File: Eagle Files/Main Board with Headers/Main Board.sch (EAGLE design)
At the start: 34 parts, among them Y1 16MHz

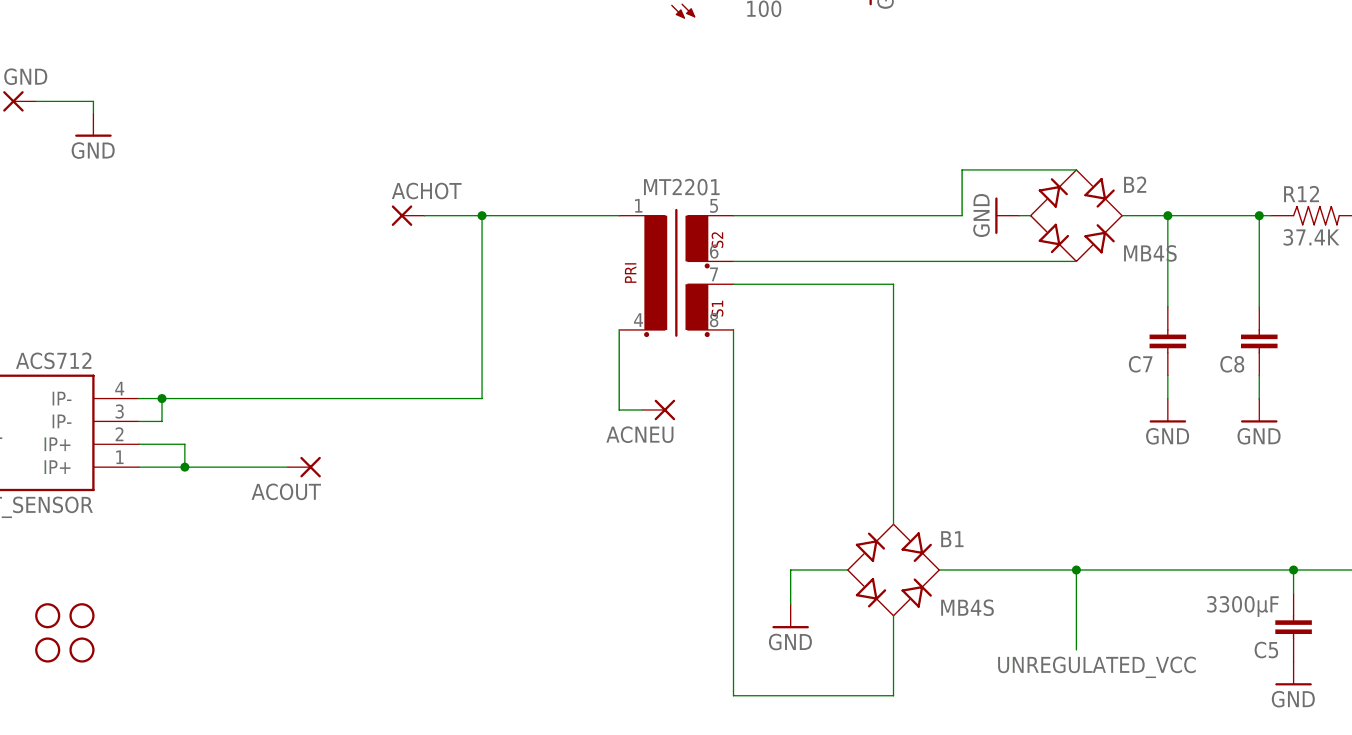
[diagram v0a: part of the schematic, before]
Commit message: More updates to the Main Board with Headers.
The transformer will now be under the board, so now we can place things inside that footprint on the top.

This saves us something around a square inch or two of board space.

--Arthur

git-svn-id: http://cd-net.net/CPE496/trunk@95 05b6d0e0-c345-4a8e-a5b7-579c8bd0b646
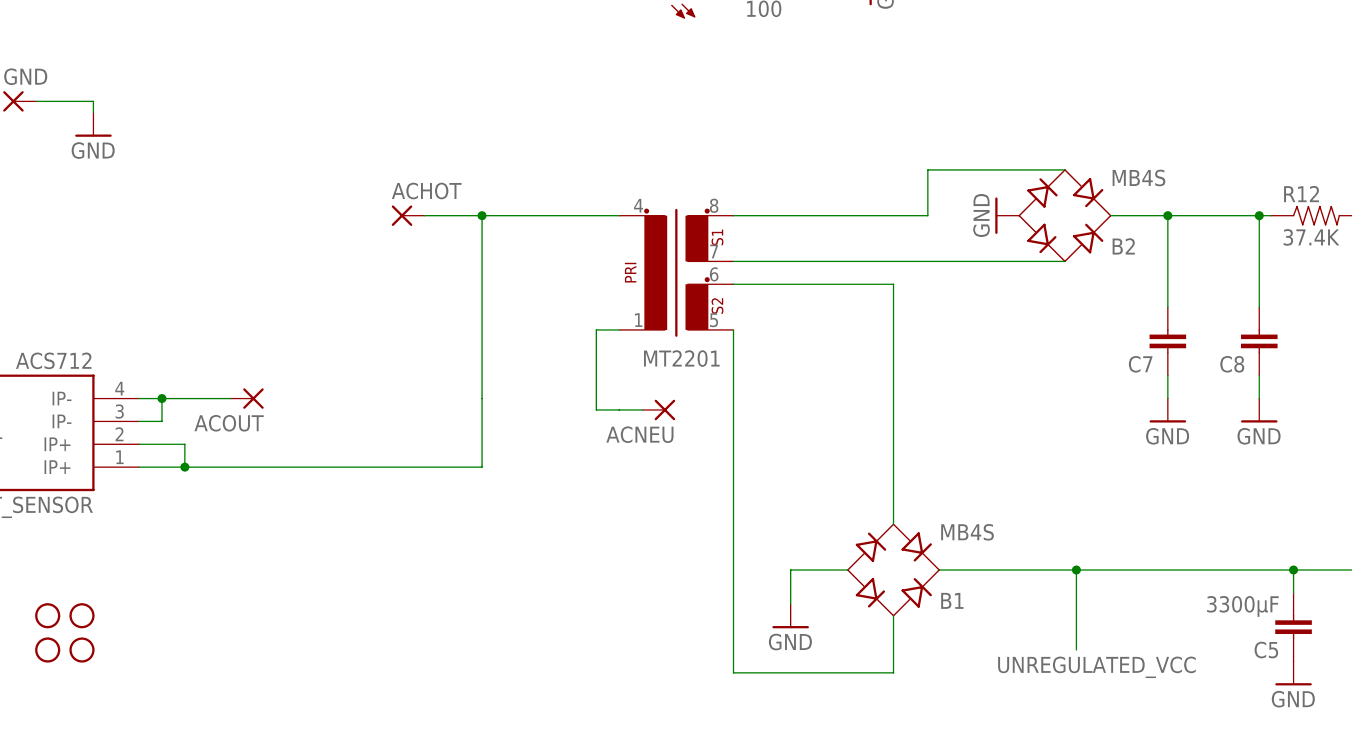
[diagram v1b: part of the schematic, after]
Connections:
- removed net N$8: ACOUT.P, CURRENT_SENSOR.IP+@1, CURRENT_SENSOR.IP+@2
- new net N$9: ACOUT.P, CURRENT_SENSOR.IP-@3, CURRENT_SENSOR.IP-@4
- net N$1: now also CURRENT_SENSOR.IP+@1, CURRENT_SENSOR.IP+@2, MT2201.4; no longer CURRENT_SENSOR.IP-@3, CURRENT_SENSOR.IP-@4, MT2201.1
- net N$2: now also MT2201.1; no longer MT2201.4
- net N$23: now also B1.AC2, MT2201.6; no longer B1.AC1, MT2201.7
- net N$3: now also B1.AC1, MT2201.5; no longer B1.AC2, MT2201.8
- net N$4: now also MT2201.7; no longer MT2201.5
- net N$5: now also MT2201.8; no longer MT2201.6
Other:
- moved on the sheet: ACOUT, B1, B2, MT2201
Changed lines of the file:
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@@
 <setting verticaltext="up"/>
 </settings>
-<grid distance="0.1" unitdist="inch" unit="inch" style="lines" multiple="1" display="no" altdistance="0.01" altunitdist="inch" altunit="inch"/>
+<grid distance="0.05" unitdist="inch" unit="inch" style="lines" multiple="1" display="yes" altdistance="0.005" altunitdist="inch" altunit="inch"/>
 <layers>
 <layer number="1" name="Top" color="4" fill="1" visible="no" active="no"/>
@@
 <instance part="R9" gate="G$1" x="-35.56" y="35.56"/>
 <instance part="GND13" gate="1" x="-25.4" y="35.56" rot="R90"/>
-<instance part="B1" gate="G$1" x="-22.86" y="-41.91"/>
+<instance part="B1" gate="G$1" x="-22.86" y="-41.91" rot="MR180"/>
 <instance part="GND14" gate="1" x="-34.29" y="-48.26"/>
 <instance part="R12" gate="G$1" x="24.13" y="-2.54"/>
@@
 <instance part="ACNEU" gate="1" x="-48.26" y="-24.13" rot="R180"/>
 <instance part="GND" gate="1" x="-120.65" y="10.16"/>
-<instance part="ACOUT" gate="1" x="-87.63" y="-30.48" rot="R180"/>
+<instance part="ACOUT" gate="1" x="-93.98" y="-22.86" rot="R180"/>
 <instance part="ISP_HEADER" gate="G$1" x="-119.38" y="66.04"/>
-<instance part="MT2201" gate="1" x="-48.26" y="-7.62"/>
+<instance part="MT2201" gate="1" x="-48.26" y="-10.16" rot="MR180"/>
 <instance part="R1" gate="G$1" x="12.7" y="111.76"/>
-<instance part="B2" gate="G$1" x="-2.54" y="-2.54"/>
+<instance part="B2" gate="G$1" x="-3.81" y="-2.54" rot="MR180"/>
 <instance part="C5" gate="G$1" x="21.59" y="-46.99" rot="R180"/>
 <instance part="C6" gate="G$1" x="33.02" y="-46.99" rot="R180"/>
@@
 <pinref part="B2" gate="G$1" pin="-"/>
 <pinref part="GND1" gate="1" pin="GND"/>
-<wire x1="-7.62" y1="-2.54" x2="-8.89" y2="-2.54" width="0.1524" layer="91"/>
 </segment>
 <segment>
@@
 <net name="N$23" class="0">
 <segment>
-<pinref part="B1" gate="G$1" pin="AC1"/>
-<pinref part="MT2201" gate="1" pin="7"/>
-<wire x1="-40.64" y1="-10.16" x2="-22.86" y2="-10.16" width="0.1524" layer="91"/>
-<wire x1="-22.86" y1="-10.16" x2="-22.86" y2="-36.83" width="0.1524" layer="91"/>
+<pinref part="MT2201" gate="1" pin="6"/>
+<wire x1="-22.86" y1="-10.16" x2="-40.64" y2="-10.16" width="0.1524" layer="91"/>
+<pinref part="B1" gate="G$1" pin="AC2"/>
+<wire x1="-22.86" y1="-36.83" x2="-22.86" y2="-10.16" width="0.1524" layer="91"/>
 </segment>
 </net>
@@
 <net name="N$2" class="0">
 <segment>
-<pinref part="MT2201" gate="1" pin="4"/>
 <pinref part="ACNEU" gate="1" pin="P"/>
-<wire x1="-53.34" y1="-15.24" x2="-53.34" y2="-24.13" width="0.1524" layer="91"/>
 <wire x1="-53.34" y1="-24.13" x2="-50.8" y2="-24.13" width="0.1524" layer="91"/>
-</segment>
-</net>
-<net name="N$3" class="0">
-<segment>
-<pinref part="MT2201" gate="1" pin="8"/>
-<wire x1="-40.64" y1="-15.24" x2="-40.64" y2="-55.88" width="0.1524" layer="91"/>
-<pinref part="B1" gate="G$1" pin="AC2"/>
-<wire x1="-40.64" y1="-55.88" x2="-22.86" y2="-55.88" width="0.1524" layer="91"/>
-<wire x1="-22.86" y1="-55.88" x2="-22.86" y2="-46.99" width="0.1524" layer="91"/>
+<wire x1="-53.34" y1="-24.13" x2="-55.88" y2="-24.13" width="0.1524" layer="91"/>
+<wire x1="-55.88" y1="-24.13" x2="-55.88" y2="-15.24" width="0.1524" layer="91"/>
+<pinref part="MT2201" gate="1" pin="1"/>
+<wire x1="-53.34" y1="-15.24" x2="-55.88" y2="-15.24" width="0.1524" layer="91"/>
 </segment>
 </net>
@@
 </segment>
 </net>
-<net name="N$4" class="0">
-<segment>
-<pinref part="B2" gate="G$1" pin="AC1"/>
-<wire x1="-2.54" y1="2.54" x2="-15.24" y2="2.54" width="0.1524" layer="91"/>
-<wire x1="-15.24" y1="2.54" x2="-15.24" y2="-2.54" width="0.1524" layer="91"/>
-<pinref part="MT2201" gate="1" pin="5"/>
-<wire x1="-15.24" y1="-2.54" x2="-40.64" y2="-2.54" width="0.1524" layer="91"/>
-</segment>
-</net>
-<net name="N$5" class="0">
-<segment>
-<pinref part="MT2201" gate="1" pin="6"/>
-<pinref part="B2" gate="G$1" pin="AC2"/>
-<wire x1="-40.64" y1="-7.62" x2="-2.54" y2="-7.62" width="0.1524" layer="91"/>
-</segment>
-</net>
 <net name="N$6" class="0">
 <segment>
 <pinref part="B2" gate="G$1" pin="+"/>
-<wire x1="2.54" y1="-2.54" x2="7.62" y2="-2.54" width="0.1524" layer="91"/>
+<wire x1="1.27" y1="-2.54" x2="7.62" y2="-2.54" width="0.1524" layer="91"/>
 <pinref part="R12" gate="G$1" pin="1"/>
 <pinref part="C8" gate="G$1" pin="2"/>
@@
 </segment>
 </net>
-<net name="N$8" class="0">
-<segment>
+<net name="N$1" class="0">
+<segment>
+<wire x1="-68.58" y1="-22.86" x2="-68.58" y2="-2.54" width="0.1524" layer="91"/>
+<pinref part="ACHOT" gate="1" pin="P"/>
+<wire x1="-74.93" y1="-2.54" x2="-68.58" y2="-2.54" width="0.1524" layer="91"/>
+<pinref part="MT2201" gate="1" pin="4"/>
+<wire x1="-53.34" y1="-2.54" x2="-68.58" y2="-2.54" width="0.1524" layer="91"/>
+<junction x="-68.58" y="-2.54"/>
 <pinref part="CURRENT_SENSOR" gate="G$1" pin="IP+@1"/>
 <wire x1="-101.6" y1="-30.48" x2="-106.68" y2="-30.48" width="0.1524" layer="91"/>
@@
 <wire x1="-106.68" y1="-27.94" x2="-101.6" y2="-27.94" width="0.1524" layer="91"/>
 <wire x1="-101.6" y1="-27.94" x2="-101.6" y2="-30.48" width="0.1524" layer="91"/>
-<pinref part="ACOUT" gate="1" pin="P"/>
-<wire x1="-90.17" y1="-30.48" x2="-101.6" y2="-30.48" width="0.1524" layer="91"/>
+<wire x1="-68.58" y1="-22.86" x2="-68.58" y2="-30.48" width="0.1524" layer="91"/>
+<wire x1="-68.58" y1="-30.48" x2="-101.6" y2="-30.48" width="0.1524" layer="91"/>
 <junction x="-101.6" y="-30.48"/>
 </segment>
 </net>
-<net name="N$1" class="0">
-<segment>
+<net name="CLKM" class="0">
+<segment>
+<pinref part="U$2" gate="G$1" pin="PD6"/>
+<wire x1="-7.62" y1="58.42" x2="-7.62" y2="40.64" width="0.1524" layer="91"/>
+<label x="-5.08" y="43.18" size="1.778" layer="95" rot="R90"/>
+</segment>
+</net>
+<net name="N/C" class="0">
+<segment>
+<pinref part="U$2" gate="G$1" pin="PD4"/>
+<wire x1="-25.4" y1="86.36" x2="-40.64" y2="86.36" width="0.1524" layer="91"/>
+<label x="-38.227" y="86.741" size="1.778" layer="95"/>
+</segment>
+</net>
+<net name="N$9" class="0">
+<segment>
+<pinref part="CURRENT_SENSOR" gate="G$1" pin="IP-@4"/>
+<pinref part="CURRENT_SENSOR" gate="G$1" pin="IP-@3"/>
 <wire x1="-106.68" y1="-25.4" x2="-104.14" y2="-25.4" width="0.1524" layer="91"/>
 <wire x1="-104.14" y1="-25.4" x2="-104.14" y2="-22.86" width="0.1524" layer="91"/>
 <wire x1="-104.14" y1="-22.86" x2="-106.68" y2="-22.86" width="0.1524" layer="91"/>
-<pinref part="CURRENT_SENSOR" gate="G$1" pin="IP-@3"/>
-<pinref part="CURRENT_SENSOR" gate="G$1" pin="IP-@4"/>
-<pinref part="MT2201" gate="1" pin="1"/>
-<wire x1="-68.58" y1="-22.86" x2="-68.58" y2="-2.54" width="0.1524" layer="91"/>
-<wire x1="-53.34" y1="-2.54" x2="-68.58" y2="-2.54" width="0.1524" layer="91"/>
-<pinref part="ACHOT" gate="1" pin="P"/>
-<wire x1="-74.93" y1="-2.54" x2="-68.58" y2="-2.54" width="0.1524" layer="91"/>
-<junction x="-68.58" y="-2.54"/>
-<wire x1="-104.14" y1="-22.86" x2="-68.58" y2="-22.86" width="0.1524" layer="91"/>
+<pinref part="ACOUT" gate="1" pin="P"/>
+<wire x1="-96.52" y1="-22.86" x2="-104.14" y2="-22.86" width="0.1524" layer="91"/>
 <junction x="-104.14" y="-22.86"/>
 </segment>
 </net>
-<net name="CLKM" class="0">
-<segment>
-<pinref part="U$2" gate="G$1" pin="PD6"/>
-<wire x1="-7.62" y1="58.42" x2="-7.62" y2="40.64" width="0.1524" layer="91"/>
-<label x="-5.08" y="43.18" size="1.778" layer="95" rot="R90"/>
-</segment>
-</net>
-<net name="N/C" class="0">
-<segment>
-<pinref part="U$2" gate="G$1" pin="PD4"/>
-<wire x1="-25.4" y1="86.36" x2="-40.64" y2="86.36" width="0.1524" layer="91"/>
-<label x="-38.227" y="86.741" size="1.778" layer="95"/>
-</segment>
-</net>
+<net name="N$4" class="0">
+<segment>
+<pinref part="B2" gate="G$1" pin="AC1"/>
+<pinref part="MT2201" gate="1" pin="7"/>
+<wire x1="-3.81" y1="-7.62" x2="-40.64" y2="-7.62" width="0.1524" layer="91"/>
+</segment>
+</net>
+<net name="N$5" class="0">
+<segment>
+<pinref part="MT2201" gate="1" pin="8"/>
+<wire x1="-40.64" y1="-2.54" x2="-19.05" y2="-2.54" width="0.1524" layer="91"/>
+<wire x1="-19.05" y1="-2.54" x2="-19.05" y2="2.54" width="0.1524" layer="91"/>
+<pinref part="B2" gate="G$1" pin="AC2"/>
+<wire x1="-19.05" y1="2.54" x2="-3.81" y2="2.54" width="0.1524" layer="91"/>
+</segment>
+</net>
+<net name="N$3" class="0">
+<segment>
+<pinref part="B1" gate="G$1" pin="AC1"/>
+<wire x1="-22.86" y1="-46.99" x2="-22.86" y2="-53.34" width="0.1524" layer="91"/>
+<wire x1="-22.86" y1="-53.34" x2="-40.64" y2="-53.34" width="0.1524" layer="91"/>
+<pinref part="MT2201" gate="1" pin="5"/>
+<wire x1="-40.64" y1="-53.34" x2="-40.64" y2="-15.24" width="0.1524" layer="91"/>
+</segment>
+</net>
